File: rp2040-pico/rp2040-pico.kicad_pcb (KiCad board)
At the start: 2 copper layers, 159.9 x 99.9 mm, 4 parts

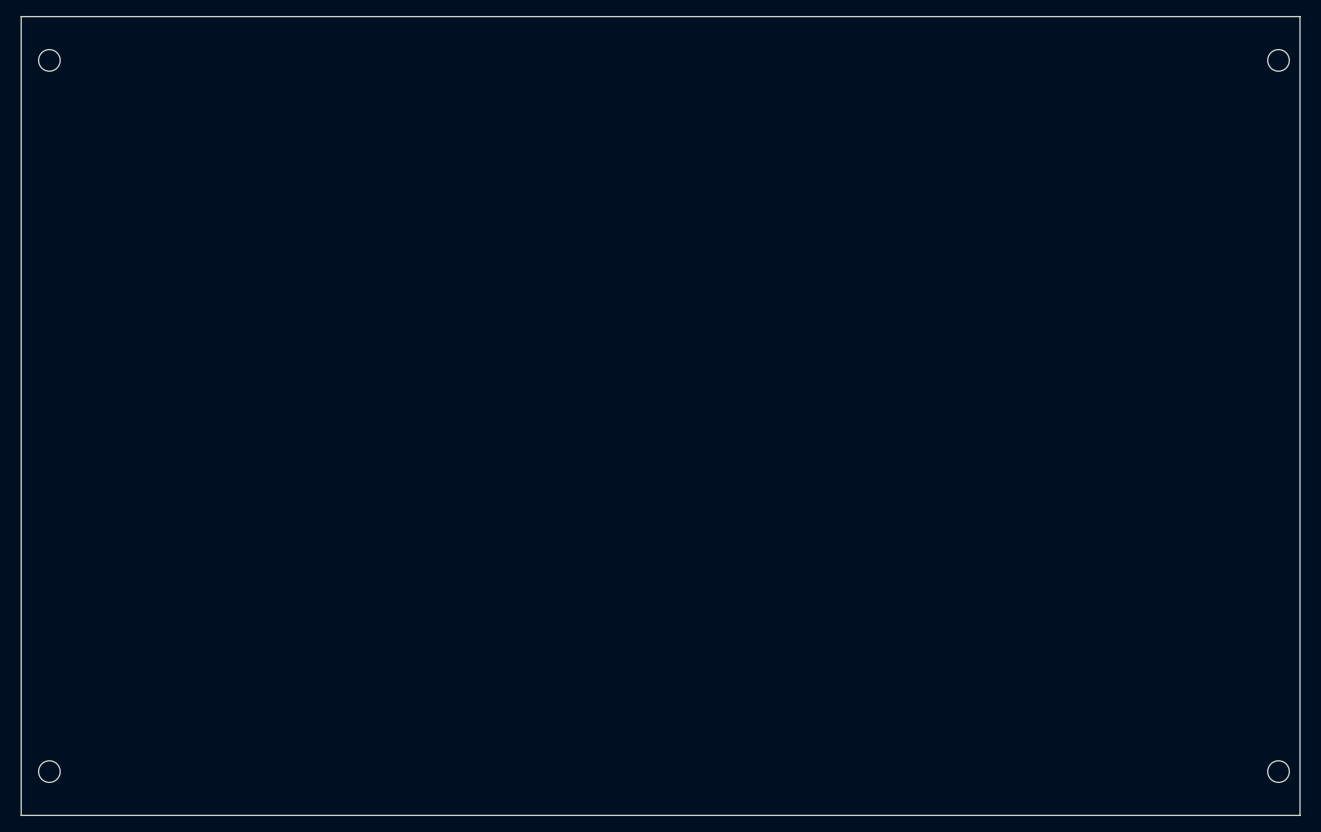
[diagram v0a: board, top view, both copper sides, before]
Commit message: Updated schematic and started PCB development
Test points have been removed from the schematic where they were found
to be unnecessary or would make efficient placement of components
impossible. Most notable the test points connected to the flash chip.
These are not required as one can just probe the pins of the flash chip
with ease.

Some nets have also been labeled to assist in PCB development.

The componets have been roughly positioned on the PCB, grouped by their
function with the RP2040 related components being mostly connected.

Signed-off-by: Matthew Nickson <mnickson@sidingsmedia.com>
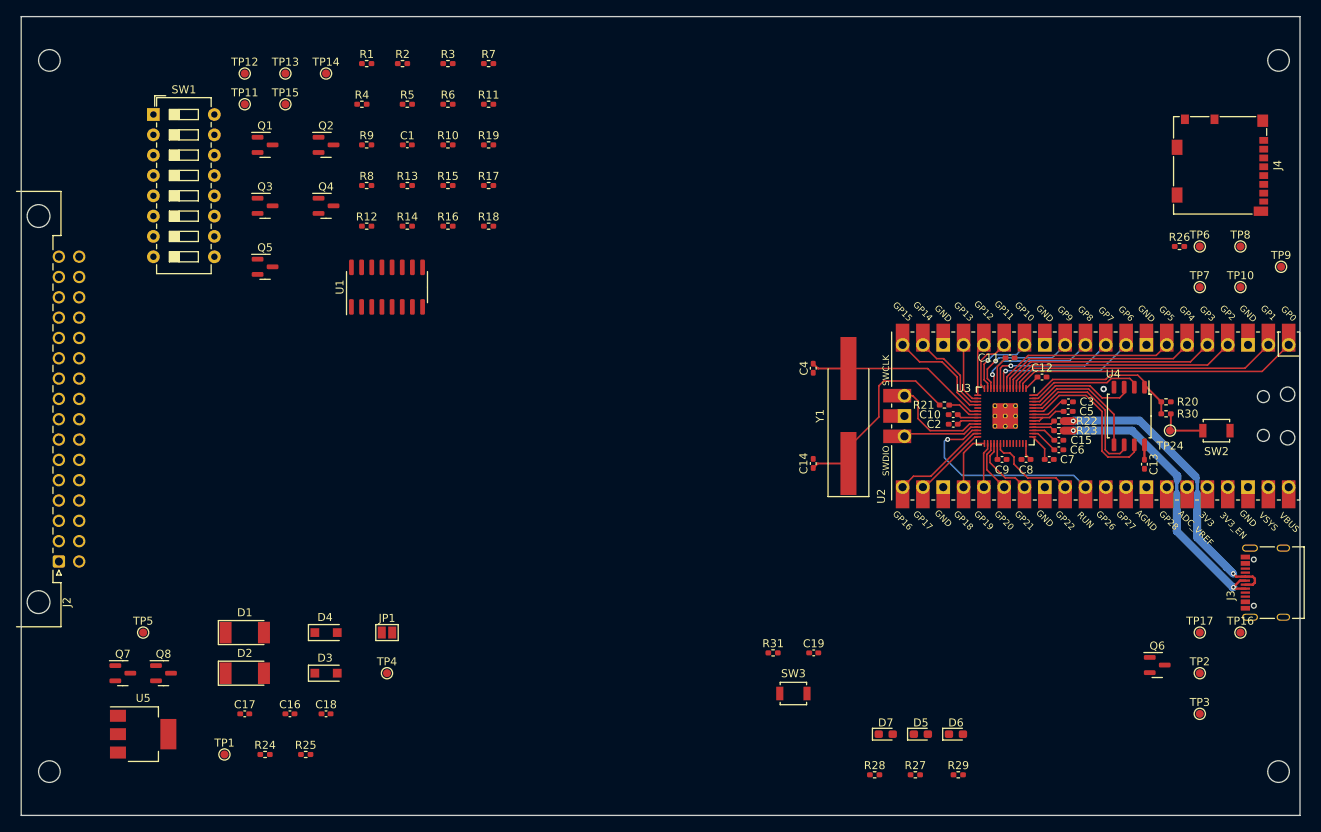
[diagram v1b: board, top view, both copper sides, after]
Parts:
- added C1: 0.1uF, Capacitor_SMD:C_0402_1005Metric_Pad0.74x0.62mm_HandSolder, F.Cu at (103.3, 61.1)
- added C10: 100n, Capacitor_SMD:C_0402_1005Metric_Pad0.74x0.62mm_HandSolder, F.Cu at (171.6, 94.8)
- added C11: 100n, Capacitor_SMD:C_0402_1005Metric_Pad0.74x0.62mm_HandSolder, F.Cu at (178.7, 87.7)
- added C12: 100n, Capacitor_SMD:C_0402_1005Metric_Pad0.74x0.62mm_HandSolder, F.Cu at (182.7, 90.1)
- added C13: 100n, Capacitor_SMD:C_0402_1005Metric_Pad0.74x0.62mm_HandSolder, F.Cu at (195.5, 101.0)
- added C14: 27p, Capacitor_SMD:C_0402_1005Metric_Pad0.74x0.62mm_HandSolder, F.Cu at (154.1, 100.9)
- added C15: 1u, Capacitor_SMD:C_0402_1005Metric_Pad0.74x0.62mm_HandSolder, F.Cu at (184.8, 98.0)
- added C16: 0.1u, Capacitor_SMD:C_0402_1005Metric_Pad0.74x0.62mm_HandSolder, F.Cu at (88.7, 132.2)
- added C17: 10u, Capacitor_SMD:C_0402_1005Metric_Pad0.74x0.62mm_HandSolder, F.Cu at (83.0, 132.2)
- added C18: 1u, Capacitor_SMD:C_0402_1005Metric_Pad0.74x0.62mm_HandSolder, F.Cu at (93.2, 132.2)
- added C19: 0.1u, Capacitor_SMD:C_0402_1005Metric_Pad0.74x0.62mm_HandSolder, F.Cu at (154.1, 124.6)
- added C2: 100n, Capacitor_SMD:C_0402_1005Metric_Pad0.74x0.62mm_HandSolder, F.Cu at (171.6, 96.0)
- added C3: 100n, Capacitor_SMD:C_0402_1005Metric_Pad0.74x0.62mm_HandSolder, F.Cu at (186.0, 93.2)
- added C4: 27p, Capacitor_SMD:C_0402_1005Metric_Pad0.74x0.62mm_HandSolder, F.Cu at (154.1, 89.0)
- added C5: 100n, Capacitor_SMD:C_0402_1005Metric_Pad0.74x0.62mm_HandSolder, F.Cu at (185.9, 94.4)
- added C6: 1u, Capacitor_SMD:C_0402_1005Metric_Pad0.74x0.62mm_HandSolder, F.Cu at (184.8, 99.2)
- added C7: 100n, Capacitor_SMD:C_0402_1005Metric_Pad0.74x0.62mm_HandSolder, F.Cu at (183.6, 100.4)
- added C8: 100n, Capacitor_SMD:C_0402_1005Metric_Pad0.74x0.62mm_HandSolder, F.Cu at (180.7, 100.4)
- added C9: 100n, Capacitor_SMD:C_0402_1005Metric_Pad0.74x0.62mm_HandSolder, F.Cu at (177.7, 100.4)
- added D1: SM4002, Diode_SMD:D_MELF, F.Cu at (83.0, 122.1)
- added D2: SM4002, Diode_SMD:D_MELF, F.Cu at (83.0, 127.2)
- added D3: MBR1020VL, Diode_SMD:D_SOD-123F, F.Cu at (93.2, 127.2)
- added D4: MBR1020VL, Diode_SMD:D_SOD-123F, F.Cu at (93.2, 122.1)
- added D5: LED, LED_SMD:LED_0603_1608Metric_Pad1.05x0.95mm_HandSolder, F.Cu at (167.5, 134.8)
- added D6: LED, LED_SMD:LED_0603_1608Metric_Pad1.05x0.95mm_HandSolder, F.Cu at (171.9, 134.8)
- added D7: LED, LED_SMD:LED_0603_1608Metric_Pad1.05x0.95mm_HandSolder, F.Cu at (163.1, 134.8)
- added J2: DIN41612_02x16_AB, Connector_DIN:DIN41612_B2_2x16_Male_Horizontal_THT, F.Cu at (59.8, 113.2)
- added J3: USB_C_Receptacle_USB2.0, Connector_USB:USB_C_Receptacle_Palconn_UTC16-G, F.Cu at (210.6, 115.8)
- added J4: Micro_SD_Card_Det, Connector_Card:microSD_HC_Molex_104031-0811, F.Cu at (204.9, 63.6)
- added JP1: Jumper_2_Open, Jumper:SolderJumper-2_P1.3mm_Open_Pad1.0x1.5mm, F.Cu at (100.8, 122.1)
- added Q1: BSS138, Package_TO_SOT_SMD:SOT-23, F.Cu at (85.6, 61.1)
- added Q2: BSS138, Package_TO_SOT_SMD:SOT-23, F.Cu at (93.2, 61.1)
- added Q3: BSS138, Package_TO_SOT_SMD:SOT-23, F.Cu at (85.6, 68.7)
- added Q4: BSS138, Package_TO_SOT_SMD:SOT-23, F.Cu at (93.2, 68.7)
- added Q5: BSS138, Package_TO_SOT_SMD:SOT-23, F.Cu at (85.6, 76.3)
- added Q6: DMG2305UX, Package_TO_SOT_SMD:SOT-23, F.Cu at (197.1, 126.1)
- added Q7: DMG2305UX, Package_TO_SOT_SMD:SOT-23, F.Cu at (67.8, 127.2)
- added Q8: DMG2305UX, Package_TO_SOT_SMD:SOT-23, F.Cu at (72.9, 127.2)
- added R1: 10K, Resistor_SMD:R_0402_1005Metric_Pad0.72x0.64mm_HandSolder, F.Cu at (98.3, 51.0)
- added R10: 1K, Resistor_SMD:R_0402_1005Metric_Pad0.72x0.64mm_HandSolder, F.Cu at (108.4, 61.1)
- added R11: 1K, Resistor_SMD:R_0402_1005Metric_Pad0.72x0.64mm_HandSolder, F.Cu at (113.5, 56.0)
- added R12: 10K, Resistor_SMD:R_0402_1005Metric_Pad0.72x0.64mm_HandSolder, F.Cu at (98.3, 71.3)
- added R13: 10K, Resistor_SMD:R_0402_1005Metric_Pad0.72x0.64mm_HandSolder, F.Cu at (103.3, 66.2)
- added R14: 1K, Resistor_SMD:R_0402_1005Metric_Pad0.72x0.64mm_HandSolder, F.Cu at (103.3, 71.3)
- added R15: 1K, Resistor_SMD:R_0402_1005Metric_Pad0.72x0.64mm_HandSolder, F.Cu at (108.4, 66.2)
- added R16: 1K, Resistor_SMD:R_0402_1005Metric_Pad0.72x0.64mm_HandSolder, F.Cu at (108.4, 71.3)
- added R17: 1K, Resistor_SMD:R_0402_1005Metric_Pad0.72x0.64mm_HandSolder, F.Cu at (113.5, 66.2)
- added R18: 10K, Resistor_SMD:R_0402_1005Metric_Pad0.72x0.64mm_HandSolder, F.Cu at (113.5, 71.3)
- added R19: 10K, Resistor_SMD:R_0402_1005Metric_Pad0.72x0.64mm_HandSolder, F.Cu at (113.5, 61.1)
- added R2: 10K, Resistor_SMD:R_0402_1005Metric_Pad0.72x0.64mm_HandSolder, F.Cu at (102.7, 51.0)
- added R20: DNF, Resistor_SMD:R_0402_1005Metric_Pad0.72x0.64mm_HandSolder, F.Cu at (198.2, 93.2)
- added R21: 1K, Resistor_SMD:R_0402_1005Metric_Pad0.72x0.64mm_HandSolder, F.Cu at (170.5, 93.6)
- added R22: 27R, Resistor_SMD:R_0402_1005Metric_Pad0.72x0.64mm_HandSolder, F.Cu at (184.8, 95.6)
- added R23: 27R, Resistor_SMD:R_0402_1005Metric_Pad0.72x0.64mm_HandSolder, F.Cu at (184.8, 96.8)
- added R24: 400R, Resistor_SMD:R_0402_1005Metric_Pad0.72x0.64mm_HandSolder, F.Cu at (85.6, 137.3)
- added R25: 240R, Resistor_SMD:R_0402_1005Metric_Pad0.72x0.64mm_HandSolder, F.Cu at (90.6, 137.3)
- added R26: 1K, Resistor_SMD:R_0402_1005Metric_Pad0.72x0.64mm_HandSolder, F.Cu at (199.9, 73.8)
- added R27: 220R, Resistor_SMD:R_0402_1005Metric_Pad0.72x0.64mm_HandSolder, F.Cu at (166.8, 139.8)
- added R28: 220R, Resistor_SMD:R_0402_1005Metric_Pad0.72x0.64mm_HandSolder, F.Cu at (161.8, 139.8)
- added R29: 220R, Resistor_SMD:R_0402_1005Metric_Pad0.72x0.64mm_HandSolder, F.Cu at (172.2, 139.8)
- added R3: 10K, Resistor_SMD:R_0402_1005Metric_Pad0.72x0.64mm_HandSolder, F.Cu at (108.4, 51.0)
- added R30: 1K, Resistor_SMD:R_0402_1005Metric_Pad0.72x0.64mm_HandSolder, F.Cu at (198.2, 94.7)
- added R31: 1K, Resistor_SMD:R_0402_1005Metric_Pad0.72x0.64mm_HandSolder, F.Cu at (149.1, 124.6)
- added R4: 10K, Resistor_SMD:R_0402_1005Metric_Pad0.72x0.64mm_HandSolder, F.Cu at (97.7, 56.0)
- added R5: 1K, Resistor_SMD:R_0402_1005Metric_Pad0.72x0.64mm_HandSolder, F.Cu at (103.3, 56.0)
- added R6: 1K, Resistor_SMD:R_0402_1005Metric_Pad0.72x0.64mm_HandSolder, F.Cu at (108.4, 56.0)
- added R7: 10K, Resistor_SMD:R_0402_1005Metric_Pad0.72x0.64mm_HandSolder, F.Cu at (113.5, 51.0)
- added R8: 10K, Resistor_SMD:R_0402_1005Metric_Pad0.72x0.64mm_HandSolder, F.Cu at (98.3, 66.2)
- added R9: 1K, Resistor_SMD:R_0402_1005Metric_Pad0.72x0.64mm_HandSolder, F.Cu at (98.3, 61.1)
- added SW1: SW_DIP_x08, Button_Switch_THT:SW_DIP_SPSTx08_Slide_6.7x21.88mm_W7.62mm_P2.54mm_LowProfile, F.Cu at (71.6, 57.3)
- added SW2: SW_Push, Button_Switch_SMD:SW_SPST_B3U-1000P, F.Cu at (204.5, 96.8)
- added SW3: SW_Push, Button_Switch_SMD:SW_SPST_B3U-1000P, F.Cu at (151.6, 129.7)
- added TP1: TestPoint, TestPoint:TestPoint_Pad_D1.0mm, F.Cu at (80.5, 137.3)
- added TP10: TestPoint, TestPoint:TestPoint_Pad_D1.0mm, F.Cu at (207.5, 78.9)
- added TP11: TestPoint, TestPoint:TestPoint_Pad_D1.0mm, F.Cu at (83.0, 56.0)
- added TP12: TestPoint, TestPoint:TestPoint_Pad_D1.0mm, F.Cu at (83.0, 52.2)
- added TP13: TestPoint, TestPoint:TestPoint_Pad_D1.0mm, F.Cu at (88.1, 52.2)
- added TP14: TestPoint, TestPoint:TestPoint_Pad_D1.0mm, F.Cu at (93.2, 52.2)
- added TP15: TestPoint, TestPoint:TestPoint_Pad_D1.0mm, F.Cu at (88.1, 56.0)
- added TP16: TestPoint, TestPoint:TestPoint_Pad_D1.0mm, F.Cu at (207.5, 122.1)
- added TP17: TestPoint, TestPoint:TestPoint_Pad_D1.0mm, F.Cu at (202.4, 122.1)
- added TP2: TestPoint, TestPoint:TestPoint_Pad_D1.0mm, F.Cu at (202.4, 127.2)
- added TP24: TestPoint, TestPoint:TestPoint_Pad_D1.0mm, F.Cu at (198.7, 96.8)
- added TP3: TestPoint, TestPoint:TestPoint_Pad_D1.0mm, F.Cu at (202.4, 132.2)
- added TP4: TestPoint, TestPoint:TestPoint_Pad_D1.0mm, F.Cu at (100.8, 127.2)
- added TP5: TestPoint, TestPoint:TestPoint_Pad_D1.0mm, F.Cu at (70.3, 122.1)
- added TP6: TestPoint, TestPoint:TestPoint_Pad_D1.0mm, F.Cu at (202.4, 73.8)
- added TP7: TestPoint, TestPoint:TestPoint_Pad_D1.0mm, F.Cu at (202.4, 78.9)
- added TP8: TestPoint, TestPoint:TestPoint_Pad_D1.0mm, F.Cu at (207.5, 73.8)
- added TP9: TestPoint, TestPoint:TestPoint_Pad_D1.0mm, F.Cu at (212.6, 76.3)
- added U1: 74151, Package_SO:SOIC-16_3.9x9.9mm_P1.27mm, F.Cu at (100.8, 78.9)
- added U2: Pico, MCU_RaspberryPi_and_Boards:RPi_Pico_SMD_TH, F.Cu at (189.4, 95.0)
- added U3: RP2040, MCU_RaspberryPi_and_Boards:RP2040-QFN-56, F.Cu at (178.1, 95.0)
- added U4: W25Q128JVS, Package_SO:SOIC-8_5.23x5.23mm_P1.27mm, F.Cu at (193.6, 95.0)
- added U5: LM317_SOT-223, Package_TO_SOT_SMD:SOT-223-3_TabPin2, F.Cu at (70.3, 134.8)
- added Y1: ABLS-12.000MHz-B4-T, Crystal:Crystal_SMD_HC49-SD_HandSoldering, F.Cu at (158.5, 95.0)
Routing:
- net /MCU/D+: track 0.00 -> 38.0 mm, vias 0 -> 2
- net /MCU/D-: track 0.00 -> 37.0 mm, vias 0 -> 2
- net /UART0_TX: track 0.00 -> 35.9 mm
- net /UART0_RX: track 0.00 -> 33.8 mm
- net /I2C_SCL: track 0.00 -> 29.2 mm
- net +3V3: track 0.00 -> 27.5 mm
- net /I2C_SDA: track 0.00 -> 27.2 mm
- net /~{RESET}: track 0.00 -> 26.0 mm, vias 0 -> 1
- net /UART1_TX: track 0.00 -> 25.1 mm
- net Net-(C14-Pad2): track 0.00 -> 25.0 mm
- net /UART1_RX: track 0.00 -> 23.1 mm
- net /MCU/CRYSTAL_IN: track 0.00 -> 23.0 mm
- net /MCU/QSPI_SS: track 0.00 -> 20.9 mm
- net /MCU/QSPI_SD3: track 0.00 -> 20.8 mm
- net /MCU/QSPI_SCLK: track 0.00 -> 19.1 mm
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
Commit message: Added rev 0.3 PCB + minor alterations to schematic
The PCB design work has been completed for rev 0.3 of the board. Some
minor changes to the schematic were made as issues were encountered
during board design. The most notable being the removal of unneccessary
test points and the addition of another P-channel mosfet to allow the 5V
rail to have two seperate power supplies.

Signed-off-by: Matthew Nickson <mnickson@sidingsmedia.com>
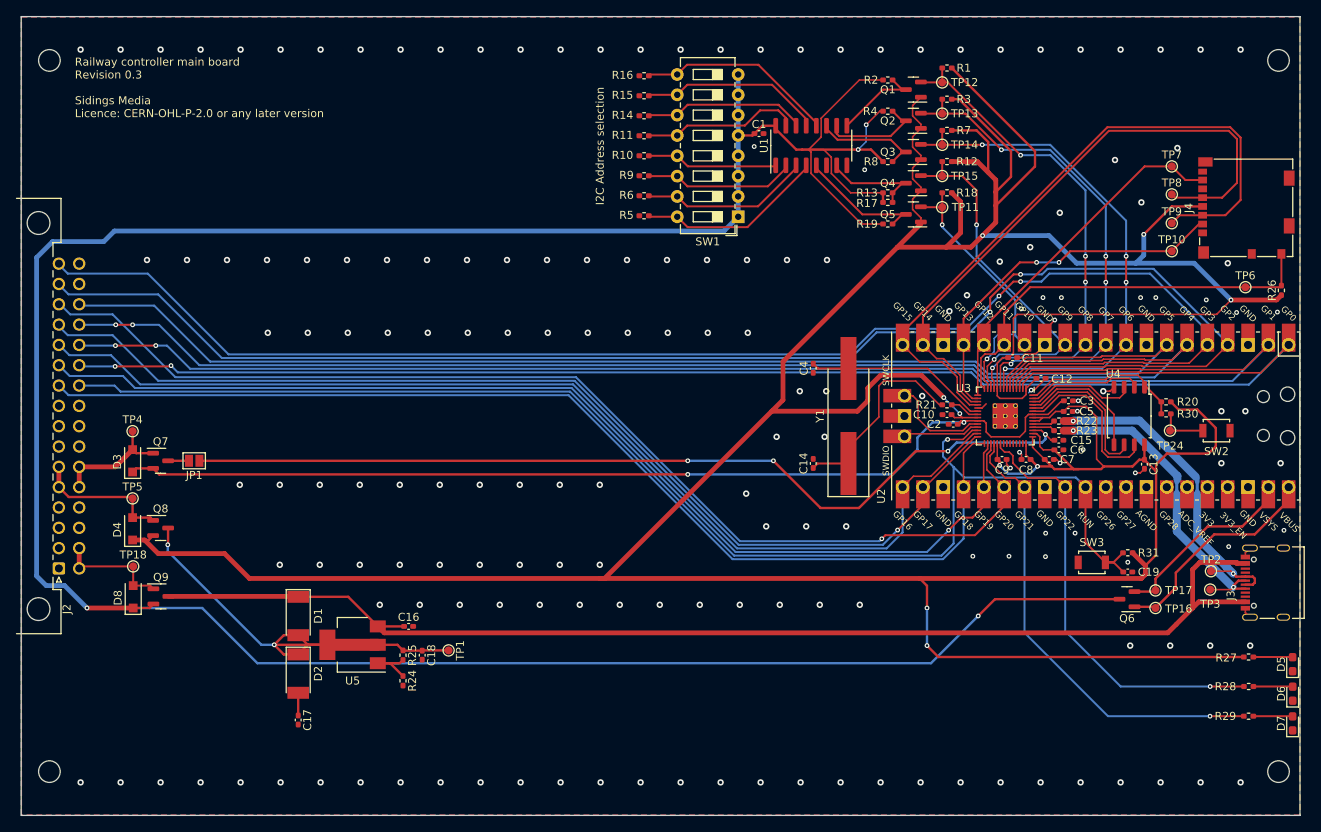
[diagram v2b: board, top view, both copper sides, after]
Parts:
- added D8: MBR1020VL, Diode_SMD:D_SOD-123F, F.Cu at (69.1, 117.6)
- added Q9: DMG2305UX, Package_TO_SOT_SMD:SOT-23, F.Cu at (72.5, 117.5)
- added TP18: TestPoint, TestPoint:TestPoint_Pad_D1.0mm, F.Cu at (69.1, 113.8)
- moved TP11 88.1 mm to (170.2, 68.9)
- moved TP12 87.2 mm to (170.2, 53.3)
- moved TP15 82.6 mm to (170.2, 65.0)
- moved TP13 82.3 mm to (170.2, 57.2)
- moved Q1 81.3 mm to (166.6, 54.2), turned to 180 degrees
- moved Q3 81.3 mm to (166.6, 62.0), turned to 180 degrees
- moved Q5 81.3 mm to (166.6, 69.8), turned to 180 degrees
- moved TP14 77.5 mm to (170.2, 61.1)
- moved SW1 74.2 mm to (144.7, 70.1), turned to 180 degrees
- moved Q2 73.5 mm to (166.6, 58.1), turned to 180 degrees
- moved Q4 73.5 mm to (166.6, 65.9), turned to 180 degrees
- moved R12 73.0 mm to (170.8, 63.2)
- moved R1 72.5 mm to (170.8, 51.5)
- moved R4 65.7 mm to (163.4, 56.9), turned to 180 degrees
- moved R8 65.2 mm to (163.4, 63.2), turned to 180 degrees
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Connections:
- J2 pad b1: +5V -> Net-(J2-Padb1)
- J2 pad b2: +5V -> Net-(J2-Padb1)
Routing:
- net +3V3: track 27.5 -> 568.2 mm, vias 0 -> 9
- net +5V: track 0.00 -> 369.9 mm, vias 0 -> 4
- net /I2C_SCL: track 29.2 -> 189.0 mm, vias 0 -> 2
- net /I2C_SDA: track 27.2 -> 184.4 mm, vias 0 -> 2
- net /UART0_TX: track 35.9 -> 190.3 mm, vias 0 -> 2
- net /VBUS: track 0.00 -> 153.3 mm
- net /UART0_RX: track 33.8 -> 186.3 mm, vias 0 -> 2
- net /~{RESET}: track 26.0 -> 170.3 mm
- net /UART1_TX: track 25.1 -> 168.1 mm, vias 0 -> 2
- net /UART1_RX: track 23.1 -> 164.1 mm
- net /~{SPI_CS2}: track 6.56 -> 141.2 mm, vias 0 -> 1
- net /SPI_MOSI: track 5.67 -> 135.7 mm, vias 0 -> 1
- net /SPI_SCLK: track 7.37 -> 137.0 mm
- net /~{SPI_CS1}: track 9.46 -> 133.1 mm, vias 0 -> 1
- net /SPI_MISO: track 12.2 -> 134.7 mm
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- added copper zone on B.Cu, net GND
- added copper zone on F.Cu, net GND
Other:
- board text added: "I2C Address selection"
- board text added: "Railway controller main board Revision 0.3 Sidings Media Licence: CERN-OHL-P-2.0 or any later version"
